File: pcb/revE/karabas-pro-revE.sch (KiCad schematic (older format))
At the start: 217 parts, among them CON1 CF-CARD, CON2 SD, CON3 VGA, CON4 Joystick, CON5 Keyboard, CON6 Mouse, CON7 Audio, CON8 12V, CON9 MicroSD', J1 Floppy, J10 Ext Joystick, J2 FPGA JTAG, J3 Floppy, J4 UART2, J5 AVR JTAG, J6 AVR UART, J7 ESP-BUS, J8 Tape In, J9 Tape Out, Q1 BC856, Q2 BC847, SW1 SW_Push, SW2 SW_Push, SW4 SW_SPST, U1 EP4CE10E22C8N, U10 ESP-12E, U11 TDA1543, U12 AMS1117-3.3, U13 AMS1117-2.5, U14 AMS1117-1.2, U15 LM2596S-5, U16 LM311, U17 74LS06, U18 74LS38, U19 CY62167EV30LL, U2 CY62167EV30LL, U20 BS62LV1600, U3 W25Q16, U3''1 W25Q16, U4 EPM3128ATC100-10N, U5 ATMEGA328-AU, U6 MB8877A, U7 TXB0104PW, U8 TXB0104PW, U9 DS1307Z+, X1 SG-7050CAN, Y1 32768Hz, Y2 16MHz

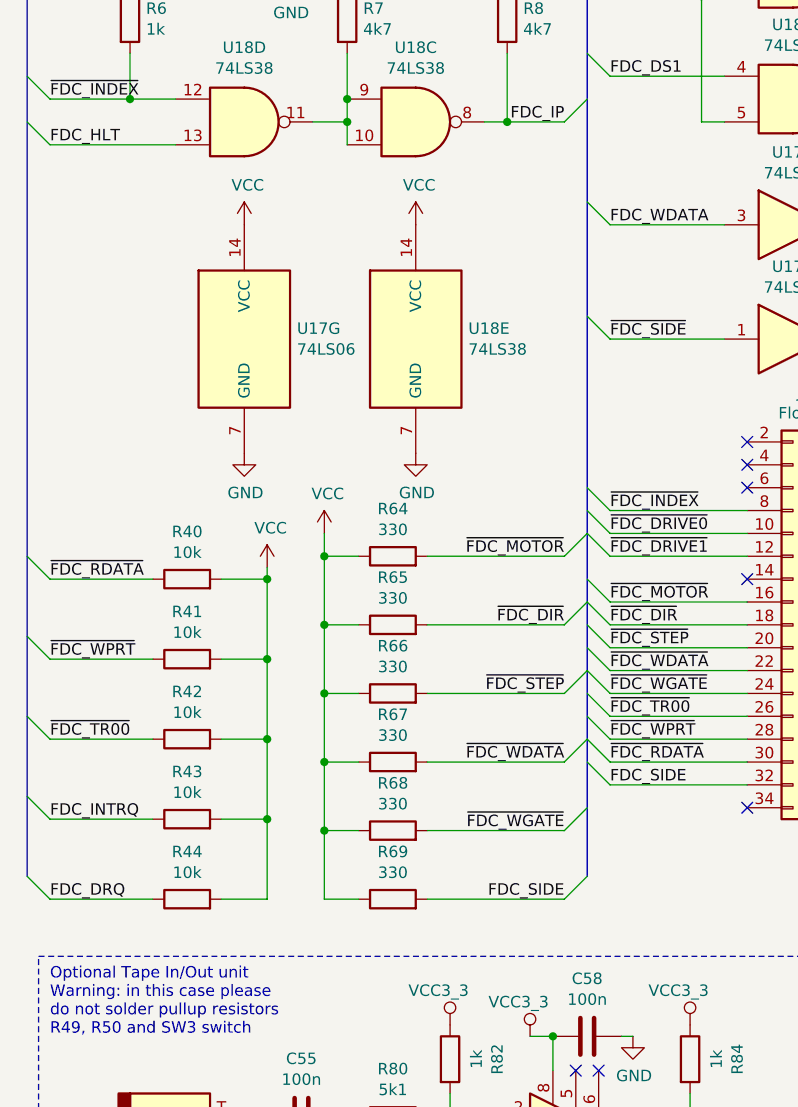
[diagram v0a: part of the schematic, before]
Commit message: Updated schematics: added note about optional terminators
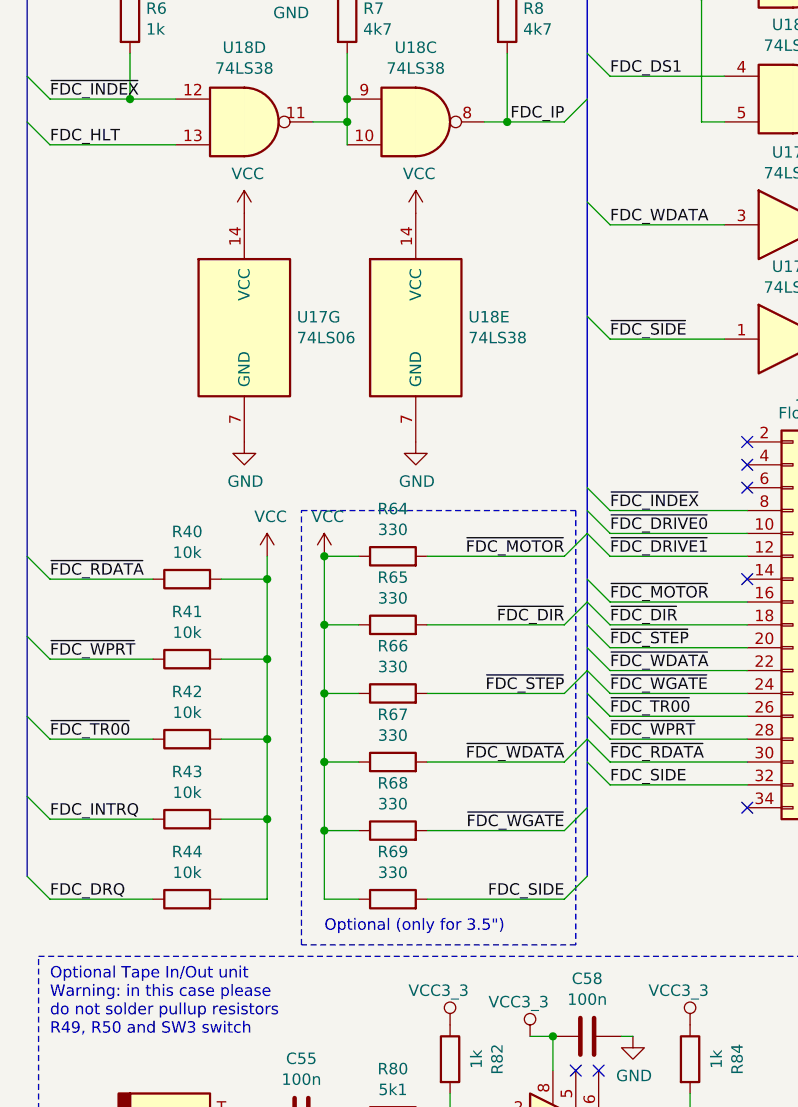
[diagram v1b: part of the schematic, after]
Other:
- note added: "Optional (only for 3.5")"
- moved on the sheet: U17G, U18E
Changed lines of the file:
@@
 L 74xx:74LS06 U17
 U 7 1 5EDDEA20
-P 1650 10650
-F 0 "U17" H 1880 10696 50  0000 L CNN
-F 1 "74LS06" H 1880 10605 50  0000 L CNN
-F 2 "Package_DIP:DIP-14_W7.62mm" H 1650 10650 50  0001 C CNN
-F 3 "http://www.ti.com/lit/gpn/sn74LS06" H 1650 10650 50  0001 C CNN
-	7    1650 10650
+P 1650 10600
+F 0 "U17" H 1880 10646 50  0000 L CNN
+F 1 "74LS06" H 1880 10555 50  0000 L CNN
+F 2 "Package_DIP:DIP-14_W7.62mm" H 1650 10600 50  0001 C CNN
+F 3 "http://www.ti.com/lit/gpn/sn74LS06" H 1650 10600 50  0001 C CNN
+	7    1650 10600
 	1    0    0    -1
 $EndComp
@@
 L 74xx:74LS38 U18
 U 5 1 5EDE4EC9
-P 2400 10650
-F 0 "U18" H 2630 10696 50  0000 L CNN
-F 1 "74LS38" H 2630 10605 50  0000 L CNN
-F 2 "Package_DIP:DIP-14_W7.62mm" H 2400 10650 50  0001 C CNN
-F 3 "http://www.ti.com/lit/gpn/sn74LS38" H 2400 10650 50  0001 C CNN
-	5    2400 10650
+P 2400 10600
+F 0 "U18" H 2630 10646 50  0000 L CNN
+F 1 "74LS38" H 2630 10555 50  0000 L CNN
+F 2 "Package_DIP:DIP-14_W7.62mm" H 2400 10600 50  0001 C CNN
+F 3 "http://www.ti.com/lit/gpn/sn74LS38" H 2400 10600 50  0001 C CNN
+	5    2400 10600
 	1    0    0    -1
 $EndComp
@@
 L power:VCC #PWR0111
 U 1 1 609C2FC1
-P 1650 10150
-F 0 "#PWR0111" H 1650 10000 50  0001 C CNN
-F 1 "VCC" H 1665 10323 50  0000 C CNN
-F 2 "" H 1650 10150 50  0001 C CNN
-F 3 "" H 1650 10150 50  0001 C CNN
-	1    1650 10150
+P 1650 10100
+F 0 "#PWR0111" H 1650 9950 50  0001 C CNN
+F 1 "VCC" H 1665 10273 50  0000 C CNN
+F 2 "" H 1650 10100 50  0001 C CNN
+F 3 "" H 1650 10100 50  0001 C CNN
+	1    1650 10100
 	1    0    0    -1
 $EndComp
@@
 L power:VCC #PWR0112
 U 1 1 609C446B
-P 2400 10150
-F 0 "#PWR0112" H 2400 10000 50  0001 C CNN
-F 1 "VCC" H 2415 10323 50  0000 C CNN
-F 2 "" H 2400 10150 50  0001 C CNN
-F 3 "" H 2400 10150 50  0001 C CNN
-	1    2400 10150
+P 2400 10100
+F 0 "#PWR0112" H 2400 9950 50  0001 C CNN
+F 1 "VCC" H 2415 10273 50  0000 C CNN
+F 2 "" H 2400 10100 50  0001 C CNN
+F 3 "" H 2400 10100 50  0001 C CNN
+	1    2400 10100
 	1    0    0    -1
 $EndComp
@@
 L power:GND #PWR0113
 U 1 1 609C4B89
-P 1650 11150
-F 0 "#PWR0113" H 1650 10900 50  0001 C CNN
-F 1 "GND" H 1655 10977 50  0000 C CNN
-F 2 "" H 1650 11150 50  0001 C CNN
-F 3 "" H 1650 11150 50  0001 C CNN
-	1    1650 11150
+P 1650 11100
+F 0 "#PWR0113" H 1650 10850 50  0001 C CNN
+F 1 "GND" H 1655 10927 50  0000 C CNN
+F 2 "" H 1650 11100 50  0001 C CNN
+F 3 "" H 1650 11100 50  0001 C CNN
+	1    1650 11100
 	1    0    0    -1
 $EndComp
@@
 L power:GND #PWR0114
 U 1 1 609C5169
-P 2400 11150
-F 0 "#PWR0114" H 2400 10900 50  0001 C CNN
-F 1 "GND" H 2405 10977 50  0000 C CNN
-F 2 "" H 2400 11150 50  0001 C CNN
-F 3 "" H 2400 11150 50  0001 C CNN
-	1    2400 11150
+P 2400 11100
+F 0 "#PWR0114" H 2400 10850 50  0001 C CNN
+F 1 "GND" H 2405 10927 50  0000 C CNN
+F 2 "" H 2400 11100 50  0001 C CNN
+F 3 "" H 2400 11100 50  0001 C CNN
+	1    2400 11100
 	1    0    0    -1
 $EndComp
@@
 L power:VCC #PWR0177
 U 1 1 5F2C0719
-P 1750 11650
-F 0 "#PWR0177" H 1750 11500 50  0001 C CNN
-F 1 "VCC" H 1765 11823 50  0000 C CNN
-F 2 "" H 1750 11650 50  0001 C CNN
-F 3 "" H 1750 11650 50  0001 C CNN
-	1    1750 11650
+P 1750 11600
+F 0 "#PWR0177" H 1750 11450 50  0001 C CNN
+F 1 "VCC" H 1765 11773 50  0000 C CNN
+F 2 "" H 1750 11600 50  0001 C CNN
+F 3 "" H 1750 11600 50  0001 C CNN
+	1    1750 11600
 	1    0    0    -1
 $EndComp
 Wire Wire Line
-	1750 11650 1750 11700
+	1750 11600 1750 11700
 Wire Wire Line
 	1750 13100 1550 13100
@@
 L power:VCC #PWR016
 U 1 1 6258E15E
-P 2000 11500
-F 0 "#PWR016" H 2000 11350 50  0001 C CNN
-F 1 "VCC" H 2015 11673 50  0000 C CNN
-F 2 "" H 2000 11500 50  0001 C CNN
-F 3 "" H 2000 11500 50  0001 C CNN
-	1    2000 11500
+P 2000 11600
+F 0 "#PWR016" H 2000 11450 50  0001 C CNN
+F 1 "VCC" H 2015 11773 50  0000 C CNN
+F 2 "" H 2000 11600 50  0001 C CNN
+F 3 "" H 2000 11600 50  0001 C CNN
+	1    2000 11600
 	1    0    0    -1
 $EndComp
-Wire Wire Line
-	2000 11500 2000 11600
 Connection ~ 2000 11600
 Text Label 8850 10050 0    50   ~ 0
@@
 Text Label 4950 9900 0    50   ~ 0
 VCC3_3
+Wire Notes Line
+	1900 11400 3100 11400
+Wire Notes Line
+	3100 11400 3100 13300
+Wire Notes Line
+	3100 13300 1900 13300
+Wire Notes Line
+	1900 13300 1900 11400
 Wire Bus Line
 	4850 6350 5350 6350
@@
 Wire Bus Line
 	6500 700  6500 15150
+Text Notes 2000 13250 0    50   ~ 0
+Optional (only for 3.5")
 $EndSCHEMATC
